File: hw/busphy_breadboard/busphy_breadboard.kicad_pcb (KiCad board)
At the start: 2 copper layers, 53.3 x 25.4 mm, 13 parts, among them J1 CONN_1, J2 CONN_1, J3 CONN_1, J4 CONN_1, J6 JUMPER, J7 CONN_2X1, J8 CONN_2X1, J9 CONN_3X1, U1 AM1S-2405, U2 MAX487

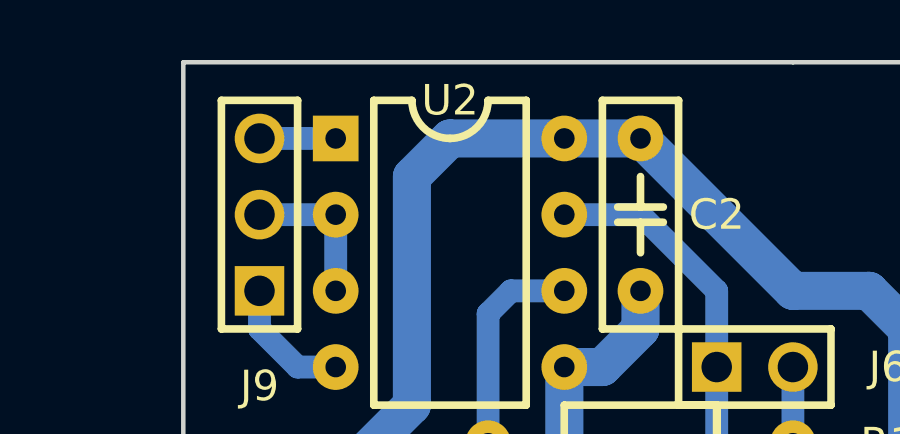
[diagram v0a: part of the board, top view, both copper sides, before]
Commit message: Update to KiCAD6: busphy_breadboard
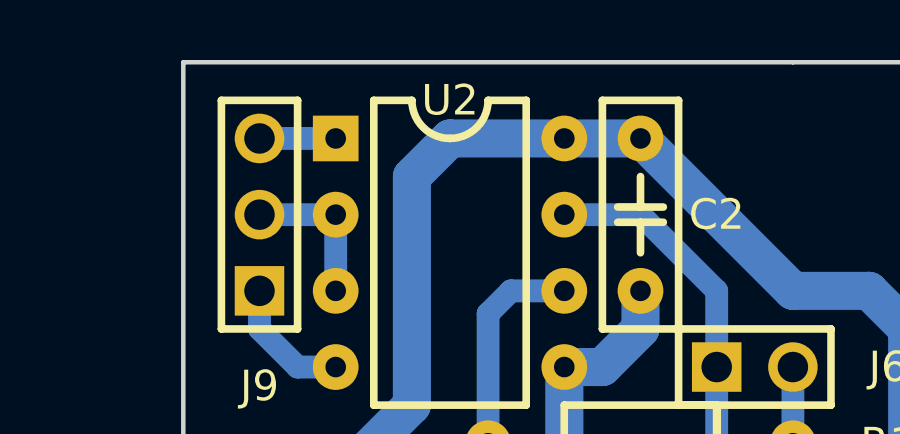
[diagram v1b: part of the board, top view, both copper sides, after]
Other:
- net class Default removed
- net class Power removed
